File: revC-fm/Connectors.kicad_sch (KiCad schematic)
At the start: 6 parts, among them J3 Conn_01x05, J4 503182-1852, J5 FTSH-105-01-F-DV-K-TR, J6 Conn_01x02, J7 Conn_01x02

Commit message: working revC
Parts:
- removed J6, J7: Conn_01x02, symbol Connector_Generic:Conn_01x02
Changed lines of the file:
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@@
   (junction (at 85.09 38.1) (diameter 0) (color 0 0 0 0)
-  )
-  (junction (at 144.78 46.99) (diameter 0) (color 0 0 0 0)
   )
   (junction (at 71.12 45.72) (diameter 0) (color 0 0 0 0)
@@
     (stroke (width 0) (type default))
   )
-  (wire (pts (xy 144.78 36.83) (xy 146.05 36.83))
-    (stroke (width 0) (type default))
-  )
   (wire (pts (xy 71.12 38.1) (xy 85.09 38.1))
     (stroke (width 0) (type default))
@@
     (stroke (width 0) (type default))
   )
-  (wire (pts (xy 144.78 46.99) (xy 144.78 49.53))
-    (stroke (width 0) (type default))
-  )
   (wire (pts (xy 74.93 114.3) (xy 69.85 114.3))
     (stroke (width 0) (type default))
@@
     (stroke (width 0) (type default))
   )
-  (wire (pts (xy 140.97 34.29) (xy 146.05 34.29))
-    (stroke (width 0) (type default))
-  )
   (wire (pts (xy 87.63 121.92) (xy 91.44 121.92))
     (stroke (width 0) (type default))
@@
     (stroke (width 0) (type default))
   )
-  (wire (pts (xy 140.97 44.45) (xy 146.05 44.45))
-    (stroke (width 0) (type default))
-  )
-  (wire (pts (xy 146.05 46.99) (xy 144.78 46.99))
-    (stroke (width 0) (type default))
-  )
   (wire (pts (xy 69.85 73.66) (xy 69.85 76.2))
     (stroke (width 0) (type default))
@@
   )
   (wire (pts (xy 69.85 116.84) (xy 74.93 116.84))
-    (stroke (width 0) (type default))
-  )
-  (wire (pts (xy 144.78 46.99) (xy 144.78 36.83))
     (stroke (width 0) (type default))
   )
@@
     )
   )
-  (global_label "VBURN1" (shape input) (at 140.97 34.29 180) (fields_autoplaced)
-    (effects (font (size 1.27 1.27) (thickness 0.254) bold) (justify right))
-    (property "Intersheetrefs" "${INTERSHEET_REFS}" (at 354.33 -1.27 0)
-      (effects (font (size 1.27 1.27)) (justify left) hide)
-    )
-  )
   (global_label "SWDIO" (shape bidirectional) (at 91.44 111.76 0) (fields_autoplaced)
     (effects (font (size 1.27 1.27)) (justify left))
     (property "Intersheetrefs" "${INTERSHEET_REFS}" (at 151.13 -54.61 0)
-      (effects (font (size 1.27 1.27)) (justify left) hide)
-    )
-  )
-  (global_label "VBURN2" (shape input) (at 140.97 44.45 180) (fields_autoplaced)
-    (effects (font (size 1.27 1.27) (thickness 0.254) bold) (justify right))
-    (property "Intersheetrefs" "${INTERSHEET_REFS}" (at 354.33 -15.24 0)
       (effects (font (size 1.27 1.27)) (justify left) hide)
     )
@@
     )
   )
-  (symbol (lib_id "mainboard:GND") (at 144.78 52.07 0) (unit 1)
-    (in_bom yes) (on_board yes) (dnp no)
-    (property "Reference" "#GND077" (at 144.78 52.07 0)
-      (effects (font (size 1.27 1.27)) hide)
-    )
-    (property "Value" "GND" (at 142.24 54.61 0)
-      (effects (font (size 1.4986 1.4986)) (justify left bottom))
-    )
-    (property "Footprint" "" (at 144.78 52.07 0)
-      (effects (font (size 1.27 1.27)) hide)
-    )
-    (property "Datasheet" "" (at 144.78 52.07 0)
-      (effects (font (size 1.27 1.27)) hide)
-    )
-    (pin "1")
-    (instances
-      (project "mainboard"
-        (path "/d1441985-7b63-4bf8-a06d-c70da2e3b78b/00000000-0000-0000-0000-00005cec60eb"
-          (reference "#GND077") (unit 1)
-        )
-      )
-    )
-  )
-  (symbol (lib_id "Connector_Generic:Conn_01x02") (at 151.13 44.45 0) (unit 1)
-    (in_bom yes) (on_board yes) (dnp no) (fields_autoplaced)
-    (property "Reference" "J7" (at 153.67 44.4499 0)
-      (effects (font (size 1.27 1.27)) (justify left))
-    )
-    (property "Value" "Conn_01x02" (at 153.67 46.9899 0)
-      (effects (font (size 1.27 1.27)) (justify left))
-    )
-    (property "Footprint" "" (at 151.13 44.45 0)
-      (effects (font (size 1.27 1.27)) hide)
-    )
-    (property "Datasheet" "~" (at 151.13 44.45 0)
-      (effects (font (size 1.27 1.27)) hide)
-    )
-    (pin "1")
-    (pin "2")
-    (instances
-      (project "mainboard"
-        (path "/d1441985-7b63-4bf8-a06d-c70da2e3b78b/00000000-0000-0000-0000-00005cec60eb"
-          (reference "J7") (unit 1)
-        )
-      )
-    )
-  )
   (symbol (lib_id "mainboard:GND") (at 69.85 127 0) (unit 1)
     (in_bom yes) (on_board yes) (dnp no)
@@
         )
       )
-    )
-  )
-  (symbol (lib_id "Connector_Generic:Conn_01x02") (at 151.13 34.29 0) (unit 1)
-    (in_bom yes) (on_board yes) (dnp no) (fields_autoplaced)
-    (property "Reference" "J6" (at 153.67 34.2899 0)
-      (effects (font (size 1.27 1.27)) (justify left))
-    )
-    (property "Value" "Conn_01x02" (at 153.67 36.8299 0)
-      (effects (font (size 1.27 1.27)) (justify left))
-    )
-    (property "Footprint" "" (at 151.13 34.29 0)
-      (effects (font (size 1.27 1.27)) hide)
-    )
-    (property "Datasheet" "~" (at 151.13 34.29 0)
-      (effects (font (size 1.27 1.27)) hide)
-    )
-    (pin "1")
-    (pin "2")
-    (instances
-      (project "mainboard"
-        (path "/d1441985-7b63-4bf8-a06d-c70da2e3b78b/00000000-0000-0000-0000-00005cec60eb"
-          (reference "J6") (unit 1)
-        )
-      )

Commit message: working revC
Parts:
- renumbered J4 to J3, J3 to J4, R135 to R107
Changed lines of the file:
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@@
   (symbol (lib_id "mainboard:503182-1852") (at 62.23 58.42 0) (mirror y) (unit 1)
     (in_bom yes) (on_board yes) (dnp no)
-    (property "Reference" "J4" (at 62.23 40.0558 0)
-      (effects (font (size 2.159 2.159)) (justify left bottom))
+    (property "Reference" "J3" (at 62.23 40.0558 0)
+      (effects (font (size 1.27 1.27)) (justify left bottom))
     )
     (property "Value" "503182-1852" (at 62.23 79.3496 0)
-      (effects (font (size 2.159 2.159)) (justify left bottom))
+      (effects (font (size 1.27 1.27)) (justify left bottom))
     )
     (property "Footprint" "mainboard:MOLEX_503182-1852" (at 62.23 58.42 0)
@@
       (project "mainboard"
         (path "/d1441985-7b63-4bf8-a06d-c70da2e3b78b/00000000-0000-0000-0000-00005cec60eb"
-          (reference "J4") (unit 1)
+          (reference "J3") (unit 1)
         )
       )
@@
   (symbol (lib_id "mainboard:GND") (at 44.45 124.46 0) (unit 1)
     (in_bom yes) (on_board yes) (dnp no)
-    (property "Reference" "#GND073" (at 44.45 124.46 0)
+    (property "Reference" "#GND057" (at 44.45 124.46 0)
       (effects (font (size 1.27 1.27)) hide)
     )
     (property "Value" "GND" (at 41.91 127 0)
-      (effects (font (size 1.4986 1.4986)) (justify left bottom))
+      (effects (font (size 1.27 1.27)) (justify left bottom))
     )
     (property "Footprint" "" (at 44.45 124.46 0)
@@
       (project "mainboard"
         (path "/d1441985-7b63-4bf8-a06d-c70da2e3b78b/00000000-0000-0000-0000-00005cec60eb"
-          (reference "#GND073") (unit 1)
+          (reference "#GND057") (unit 1)
         )
       )
@@
   (symbol (lib_id "mainboard-rescue:Conn_01x05-Connector_Generic-mainboard-rescue") (at 54.61 116.84 0) (unit 1)
     (in_bom yes) (on_board yes) (dnp no)
-    (property "Reference" "J3" (at 53.34 109.22 0)
+    (property "Reference" "J4" (at 53.34 109.22 0)
       (effects (font (size 1.27 1.27)) (justify left))
     )
@@
       (project "mainboard"
         (path "/d1441985-7b63-4bf8-a06d-c70da2e3b78b/00000000-0000-0000-0000-00005cec60eb"
-          (reference "J3") (unit 1)
+          (reference "J4") (unit 1)
         )
       )
@@
   (symbol (lib_id "mainboard:3.3V") (at 44.45 111.76 0) (unit 1)
     (in_bom yes) (on_board yes) (dnp no)
-    (property "Reference" "#SUPPLY027" (at 44.45 111.76 0)
+    (property "Reference" "#SUPPLY016" (at 44.45 111.76 0)
       (effects (font (size 1.27 1.27)) hide)
     )
     (property "Value" "3.3V" (at 43.434 108.204 0)
-      (effects (font (size 1.4986 1.4986)) (justify left bottom))
+      (effects (font (size 1.27 1.27)) (justify left bottom))
     )
     (property "Footprint" "" (at 44.45 111.76 0)
@@
       (project "mainboard"
         (path "/d1441985-7b63-4bf8-a06d-c70da2e3b78b/00000000-0000-0000-0000-00005cec60eb"
-          (reference "#SUPPLY027") (unit 1)
+          (reference "#SUPPLY016") (unit 1)
         )
       )
@@
   (symbol (lib_id "Device:R_US") (at 71.12 41.91 0) (mirror x) (unit 1)
     (in_bom yes) (on_board yes) (dnp no)
-    (property "Reference" "R135" (at 68.58 39.37 0)
+    (property "Reference" "R107" (at 68.58 39.37 0)
       (effects (font (size 1.27 1.27)))
     )
@@
       (project "mainboard"
         (path "/d1441985-7b63-4bf8-a06d-c70da2e3b78b/00000000-0000-0000-0000-00005cec60eb"
-          (reference "R135") (unit 1)
+          (reference "R107") (unit 1)
         )
       )
@@
   (symbol (lib_id "mainboard:GND") (at 85.09 78.74 0) (unit 1)
     (in_bom yes) (on_board yes) (dnp no)
-    (property "Reference" "#GND076" (at 85.09 78.74 0)
+    (property "Reference" "#GND056" (at 85.09 78.74 0)
       (effects (font (size 1.27 1.27)) hide)
     )
     (property "Value" "GND" (at 82.55 81.28 0)
-      (effects (font (size 1.4986 1.4986)) (justify left bottom))
+      (effects (font (size 1.27 1.27)) (justify left bottom))
     )
     (property "Footprint" "" (at 85.09 78.74 0)
@@
       (project "mainboard"
         (path "/d1441985-7b63-4bf8-a06d-c70da2e3b78b/00000000-0000-0000-0000-00005cec60eb"
-          (reference "#GND076") (unit 1)
+          (reference "#GND056") (unit 1)
         )
       )
@@
   (symbol (lib_id "mainboard:GND") (at 69.85 78.74 0) (unit 1)
     (in_bom yes) (on_board yes) (dnp no)
-    (property "Reference" "#GND074" (at 69.85 78.74 0)
+    (property "Reference" "#GND055" (at 69.85 78.74 0)
       (effects (font (size 1.27 1.27)) hide)
     )
     (property "Value" "GND" (at 67.31 81.28 0)
-      (effects (font (size 1.4986 1.4986)) (justify left bottom))
+      (effects (font (size 1.27 1.27)) (justify left bottom))
     )
     (property "Footprint" "" (at 69.85 78.74 0)
@@
       (project "mainboard"
         (path "/d1441985-7b63-4bf8-a06d-c70da2e3b78b/00000000-0000-0000-0000-00005cec60eb"
-          (reference "#GND074") (unit 1)
+          (reference "#GND055") (unit 1)
         )
       )
@@
   (symbol (lib_id "mainboard:3.3V") (at 85.09 36.83 0) (unit 1)
     (in_bom yes) (on_board yes) (dnp no)
-    (property "Reference" "#SUPPLY029" (at 85.09 36.83 0)
+    (property "Reference" "#SUPPLY015" (at 85.09 36.83 0)
       (effects (font (size 1.27 1.27)) hide)
     )
     (property "Value" "3.3V" (at 84.074 33.274 0)
-      (effects (font (size 1.4986 1.4986)) (justify left bottom))
+      (effects (font (size 1.27 1.27)) (justify left bottom))
     )
     (property "Footprint" "" (at 85.09 36.83 0)
@@
       (project "mainboard"
         (path "/d1441985-7b63-4bf8-a06d-c70da2e3b78b/00000000-0000-0000-0000-00005cec60eb"
-          (reference "#SUPPLY029") (unit 1)
+          (reference "#SUPPLY015") (unit 1)
         )
       )
@@
   (symbol (lib_id "mainboard:3.3V") (at 69.85 111.76 0) (unit 1)
     (in_bom yes) (on_board yes) (dnp no)
-    (property "Reference" "#SUPPLY028" (at 69.85 111.76 0)
+    (property "Reference" "#SUPPLY017" (at 69.85 111.76 0)
       (effects (font (size 1.27 1.27)) hide)
     )
     (property "Value" "3.3V" (at 68.834 108.204 0)
-      (effects (font (size 1.4986 1.4986)) (justify left bottom))
+      (effects (font (size 1.27 1.27)) (justify left bottom))
     )
     (property "Footprint" "" (at 69.85 111.76 0)
@@
       (project "mainboard"
         (path "/d1441985-7b63-4bf8-a06d-c70da2e3b78b/00000000-0000-0000-0000-00005cec60eb"
-          (reference "#SUPPLY028") (unit 1)
+          (reference "#SUPPLY017") (unit 1)
         )
       )
@@
   (symbol (lib_id "mainboard:GND") (at 69.85 127 0) (unit 1)
     (in_bom yes) (on_board yes) (dnp no)
-    (property "Reference" "#GND075" (at 69.85 127 0)
+    (property "Reference" "#GND058" (at 69.85 127 0)
       (effects (font (size 1.27 1.27)) hide)
     )
     (property "Value" "GND" (at 67.31 129.54 0)
-      (effects (font (size 1.4986 1.4986)) (justify left bottom))
+      (effects (font (size 1.27 1.27)) (justify left bottom))
     )
     (property "Footprint" "" (at 69.85 127 0)
@@
       (project "mainboard"
         (path "/d1441985-7b63-4bf8-a06d-c70da2e3b78b/00000000-0000-0000-0000-00005cec60eb"
-          (reference "#GND075") (unit 1)
-        )
-      )
+          (reference "#GND058") (unit 1)
+        )
+      )

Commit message: working revC
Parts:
- J6: renamed from J4; symbol mainboard-rescue:Conn_01x05-Connector_Generic-mainboard-rescue -> Connector_Generic:Conn_01x05; DNI DNI -> (none)
- J8: renamed from J3; value 503182-1852 -> 5031821852; footprint mainboard:MOLEX_503182-1852 -> SierraLobo:MOLEX_503182-1852; symbol mainboard:503182-1852 -> SierraLobo:503182-1852; Flight 5031821852 -> (none); Manufacturer_Name Molex -> (none); Manufacturer_Part_Number 5031821852 -> (none); Proto 5031821852 -> (none)
- renumbered J5 to J7, R107 to R197
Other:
- note removed: "NOTE: Components labeled "do not install" (DNI) are not populated by default"
- moved on the sheet: J6, J7

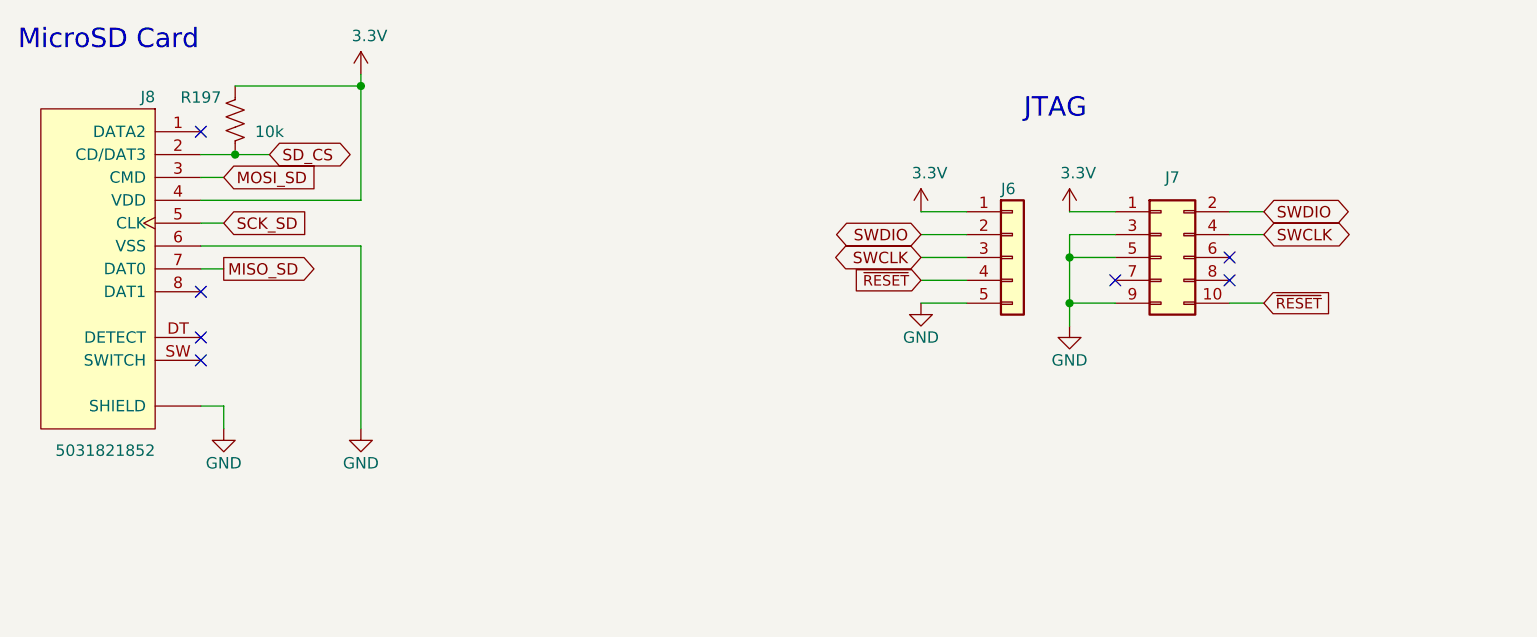
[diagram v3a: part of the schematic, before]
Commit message: updated analog , solar comp, layout
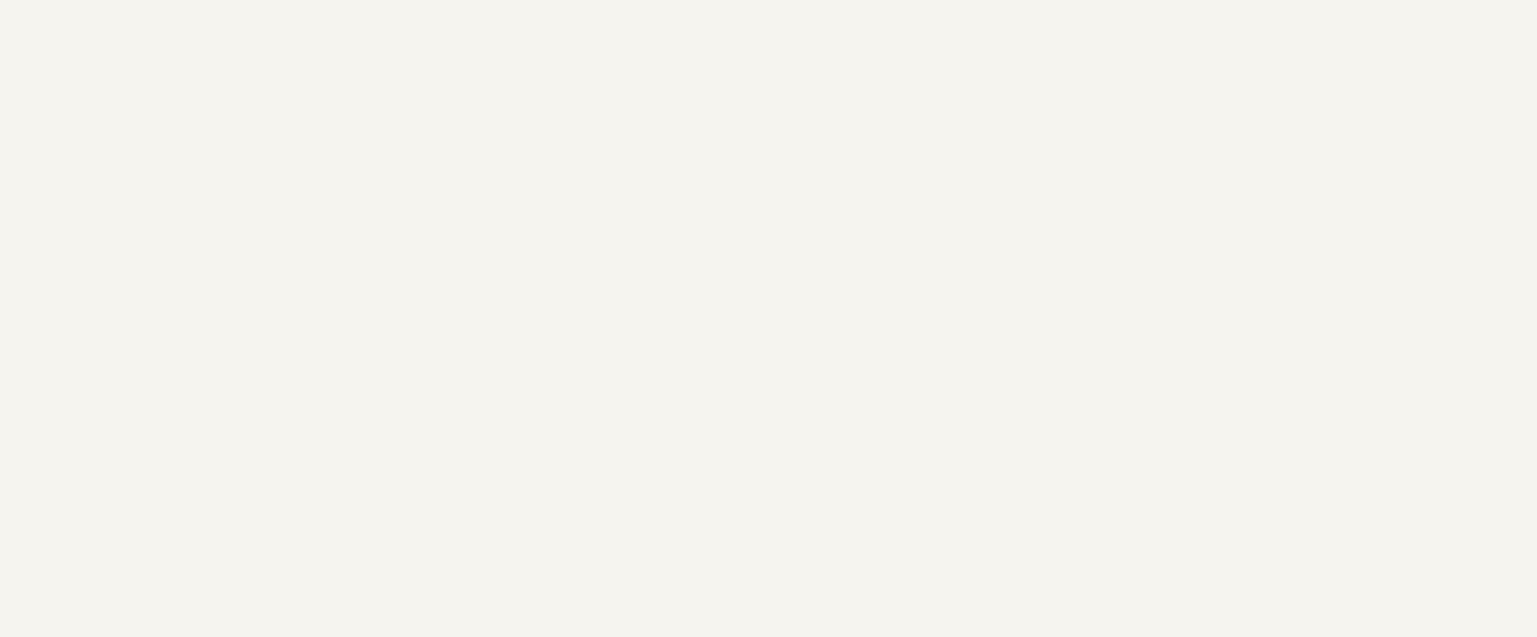
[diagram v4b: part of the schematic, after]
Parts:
- removed J6: Conn_01x05, Connector_PinHeader_2.54mm:PinHeader_1x05_P2.54mm_Vertical, symbol Connector_Generic:Conn_01x05
- removed J7: FTSH-105-01-F-DV-K-TR, Connector_PinHeader_1.27mm:PinHeader_2x05_P1.27mm_Vertical_SMD, symbol Connector_Generic:Conn_02x05_Odd_Even
- removed J8: 5031821852, SierraLobo:MOLEX_503182-1852, symbol SierraLobo:503182-1852
- removed R197: 10k, Resistor_SMD:R_0603_1608Metric, symbol Device:R_US
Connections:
- no-connect marks 7 -> 0
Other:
- note removed: "JTAG"
- note removed: "MicroSD Card"
